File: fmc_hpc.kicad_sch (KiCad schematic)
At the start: 24 parts, among them J5 ASP-134486-01

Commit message: Assign and fanout on FPGA and FMC for bank 15 signals
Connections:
- net FMC_IO_0: now also J5.G33 (LA31_P)
- net FMC_IO_10_N: now also J5.H26 (LA21_N)
- net FMC_IO_10_P: now also J5.H25 (LA21_P)
- net FMC_IO_11_N: now also J5.J13 (HA11_N)
- net FMC_IO_11_P: now also J5.J12 (HA11_P)
- net FMC_IO_12_N: now also J5.K11 (HA06_N)
- net FMC_IO_12_P: now also J5.K10 (HA06_P)
- net FMC_IO_13_N: now also J5.J10 (HA07_N)
- net FMC_IO_13_P: now also J5.J9 (HA07_P)
- net FMC_IO_14_N: now also J5.K14 (HA10_N)
- net FMC_IO_14_P: now also J5.K13 (HA10_P)
- net FMC_IO_15_N: now also J5.K20 (HA21_N)
- net FMC_IO_15_P: now also J5.K19 (HA21_P)
- net FMC_IO_16_N: now also J5.J22 (HA22_N)
- net FMC_IO_16_P: now also J5.J21 (HA22_P)
- net FMC_IO_17_N: now also J5.J7 (HA03_N)
- net FMC_IO_17_P: now also J5.J6 (HA03_P)
- net FMC_IO_18_N: now also J5.K23 (HA23_N)
- net FMC_IO_18_P: now also J5.K22 (HA23_P)
- net FMC_IO_19_N: now also J5.H23 (LA19_N)
- net FMC_IO_19_P: now also J5.H22 (LA19_P)
- net FMC_IO_1_N: now also J5.G22 (LA20_N)
- net FMC_IO_1_P: now also J5.G21 (LA20_P)
- net FMC_IO_20_N: now also J5.J16 (HA14_N)
- net FMC_IO_20_P: now also J5.J15 (HA14_P)
- net FMC_IO_21_N: now also J5.J25 (HB01_N)
- net FMC_IO_21_P: now also J5.J24 (HB01_P)
- net FMC_IO_22_N: now also J5.H32 (LA28_N)
- net FMC_IO_22_P: now also J5.H31 (LA28_P)
- net FMC_IO_23_N: now also J5.K26 (HB00_N_CC)
- net FMC_IO_23_P: now also J5.K25 (HB00_P_CC)
- net FMC_IO_24_N: now also J5.K17 (HA17_N_CC)
- net FMC_IO_24_P: now also J5.K16 (HA17_P_CC)
- net FMC_IO_25: now also J5.J18 (HA18_P)
- net FMC_IO_2_N: now also J5.G19 (LA16_N)
- net FMC_IO_2_P: now also J5.G18 (LA16_P)
- net FMC_IO_3_N: now also J5.H20 (LA15_N)
- net FMC_IO_3_P: now also J5.H19 (LA15_P)
- net FMC_IO_4_N: now also J5.H17 (LA11_N)
- net FMC_IO_4_P: now also J5.H16 (LA11_P)
- net FMC_IO_5_N: now also J5.K8 (HA02_N)
- net FMC_IO_5_P: now also J5.K7 (HA02_P)
- net FMC_IO_6_N: now also J5.G25 (LA22_N)
- net FMC_IO_6_P: now also J5.G24 (LA22_P)
- net FMC_IO_7_N: now also J5.H29 (LA24_N)
- net FMC_IO_7_P: now also J5.H28 (LA24_P)
- net FMC_IO_8_N: now also J5.G28 (LA25_N)
- net FMC_IO_8_P: now also J5.G27 (LA25_P)
- net FMC_IO_9_N: now also J5.G31 (LA29_N)
- net FMC_IO_9_P: now also J5.G30 (LA29_P)
- net GND: no longer C258.2
- net VIN: no longer C258.1
- no-connect marks 19 -> 24
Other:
- moved on the sheet: C257, C258, D18, J5B, J5D, R208, R209

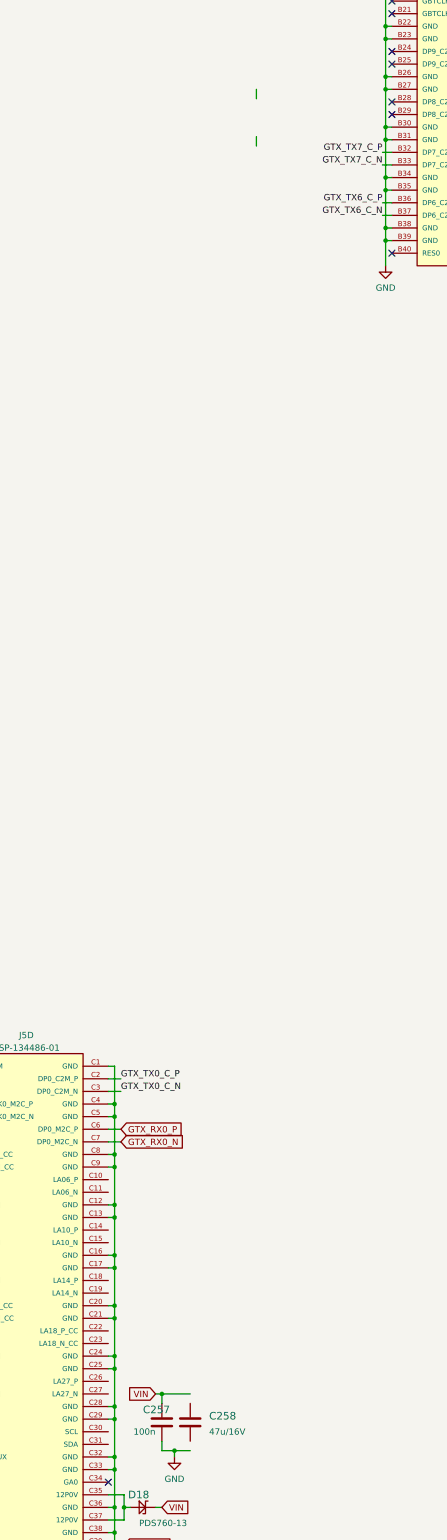
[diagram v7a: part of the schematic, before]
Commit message: Progress in FMC routing
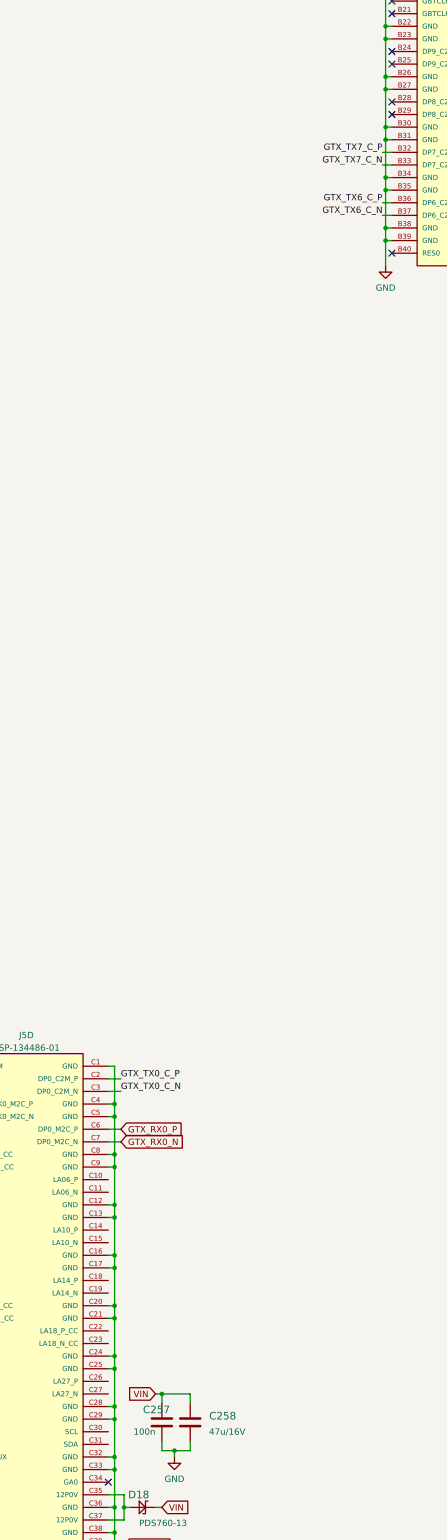
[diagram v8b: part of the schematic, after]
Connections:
- net GND: now also C258.2
- net VIN: now also C258.1
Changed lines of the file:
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@@
     (stroke (width 0) (type default) (color 0 0 0 0))
   )
-  (wire (pts (xy 262.89 132.715) (xy 262.89 134.62))
+  (wire (pts (xy 249.555 395.605) (xy 249.555 397.51))
     (stroke (width 0) (type default) (color 0 0 0 0))
   )
@@
     (stroke (width 0) (type default) (color 0 0 0 0))
   )
-  (wire (pts (xy 262.89 142.24) (xy 262.89 144.145))
-    (stroke (width 0) (type default) (color 0 0 0 0))
-  )
+  (wire (pts (xy 249.555 405.13) (xy 249.555 407.035))
+    (stroke (width 0) (type default) (color 0 0 0 0))
+  )
